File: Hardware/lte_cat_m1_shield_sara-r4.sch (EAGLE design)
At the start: 81 parts, among them J8 U.FL, J9 NANO_SIM, Q1 2.5A/30V/105mΩ, Q2 600mA/40V, U1 TXB0104, U2 AP2112K-3.3, U3 MCP73831, U4 TCA9406DCU, U5 AP7361C-33FGE, U6 SARA-R410M-2B

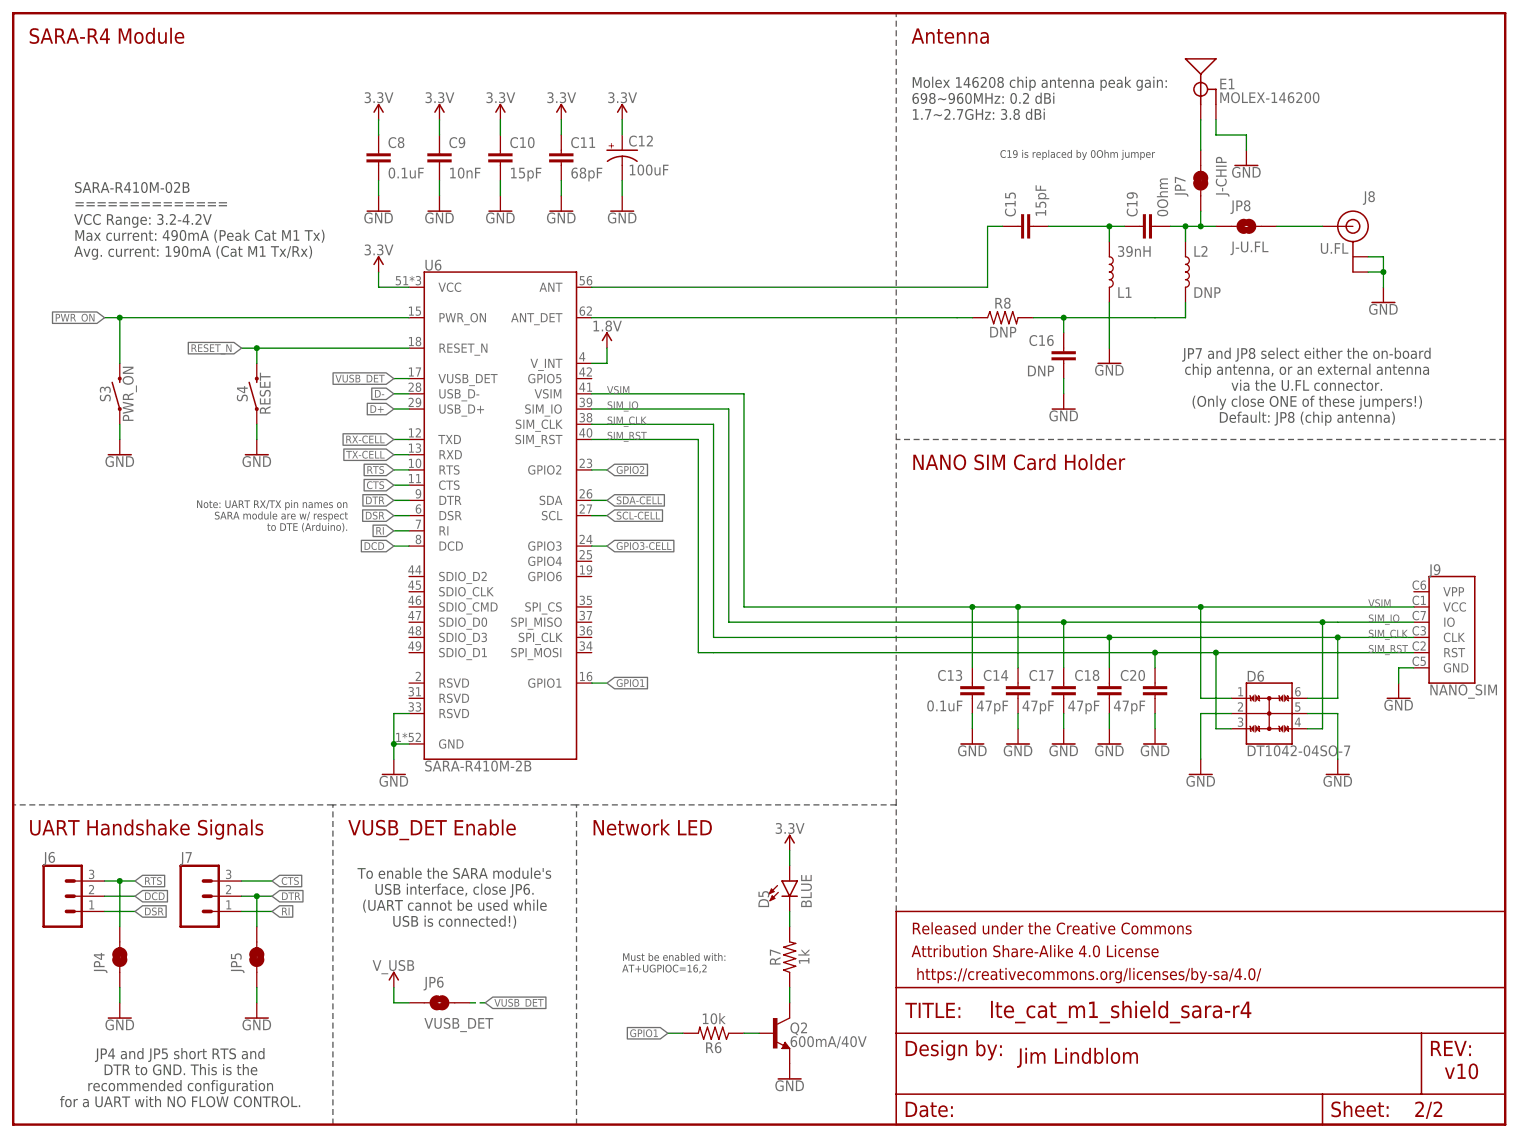
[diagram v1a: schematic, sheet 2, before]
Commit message: Revising product name in silk, schematic fixes.
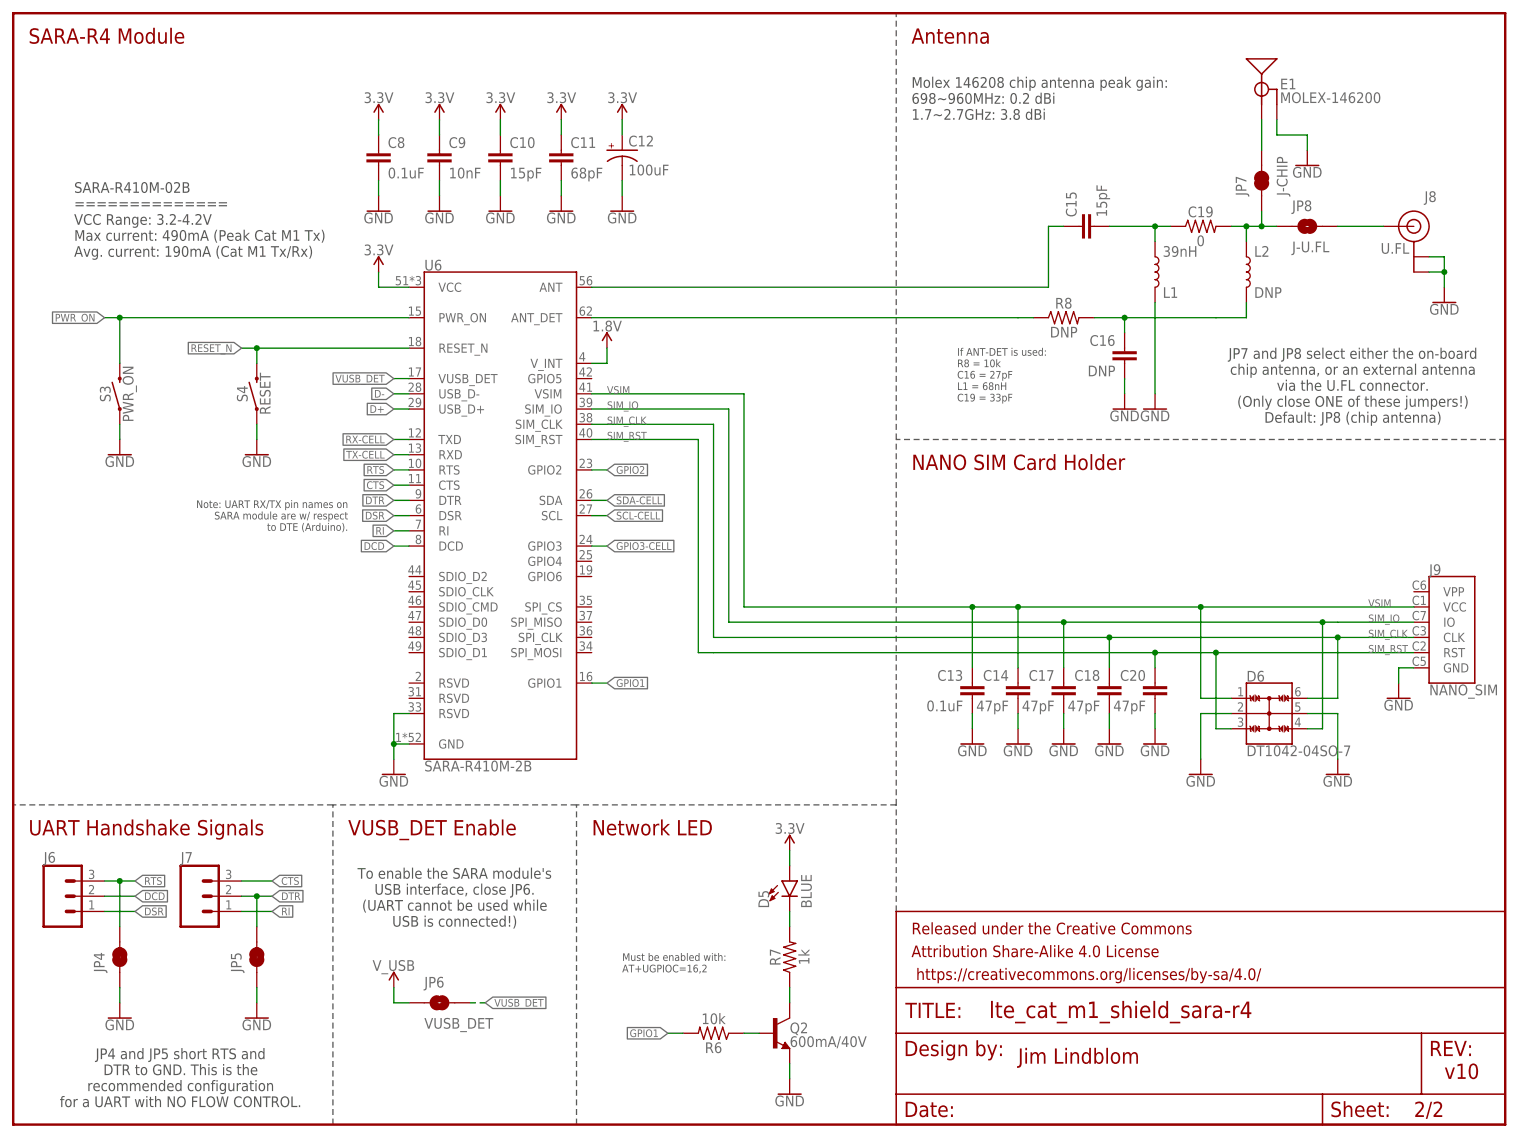
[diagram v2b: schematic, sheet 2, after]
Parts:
- C19: value 0Ohm -> 0; device SparkFun-Capacitors:33PF-0603-50V-5% -> SparkFun-Resistors:0OHM-0603-1/10W-5%
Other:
- note added: "If ANT-DET is used: R8 = 10k C16 = 27pF L1 = 68nH C19 = 33pF"
- note removed: "C19 is replaced by 0Ohm jumper"
- moved on the sheet: C15, C16, E1, J8, JP7, JP8, L1, L2, R8

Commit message: Disconnected AREF from GND
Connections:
- net GND: no longer B1.AREF
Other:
- note added: "v11"
